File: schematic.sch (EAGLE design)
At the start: 24 parts, among them IC1 ATMEGA168-20P, IC2 7805T, IC3 REG1117

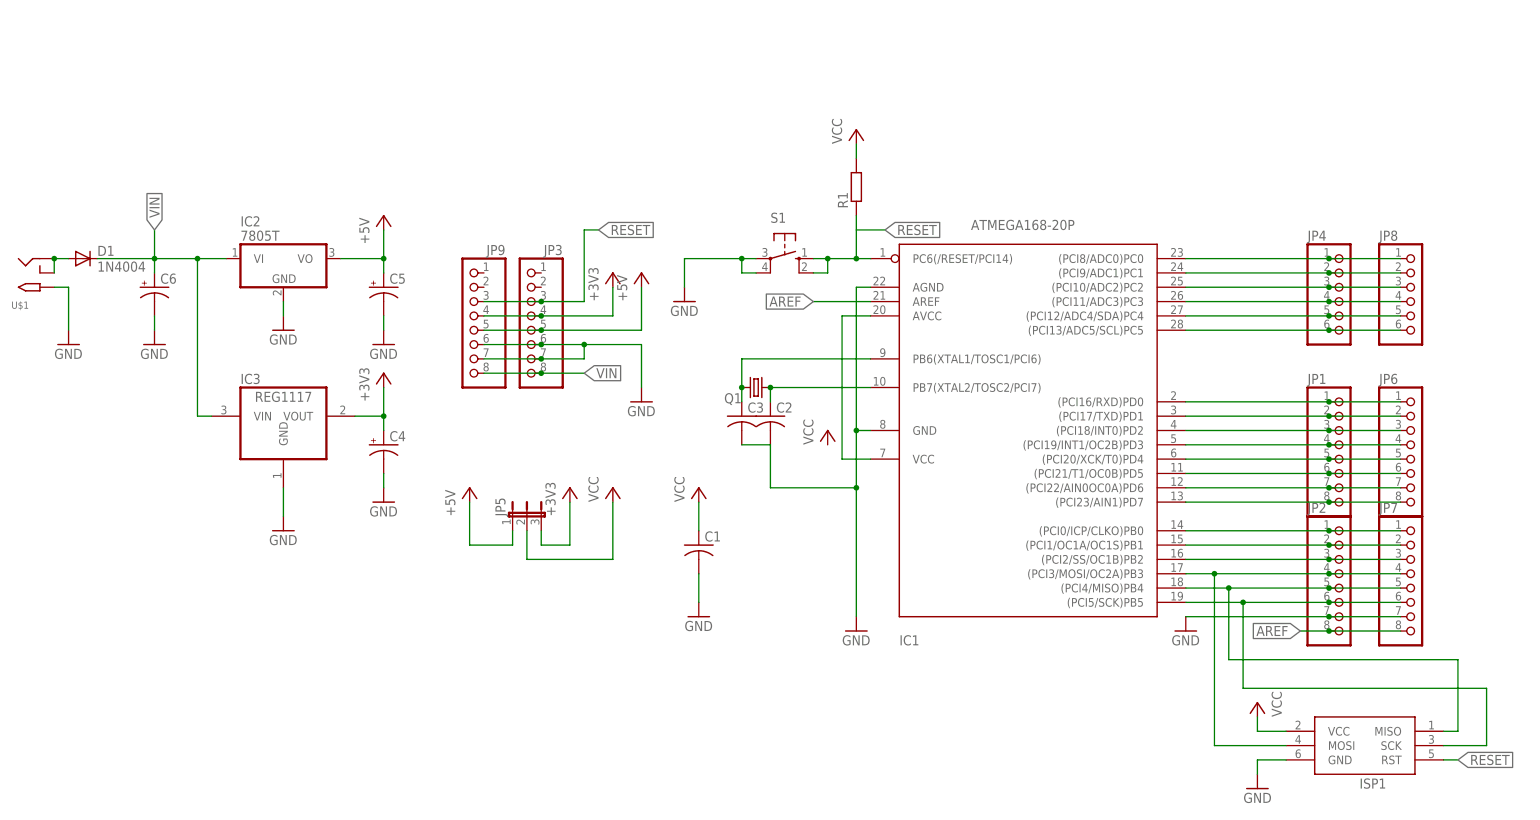
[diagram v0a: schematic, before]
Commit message: Small fixes
Added a serial port header and LEDs for on and pin 13
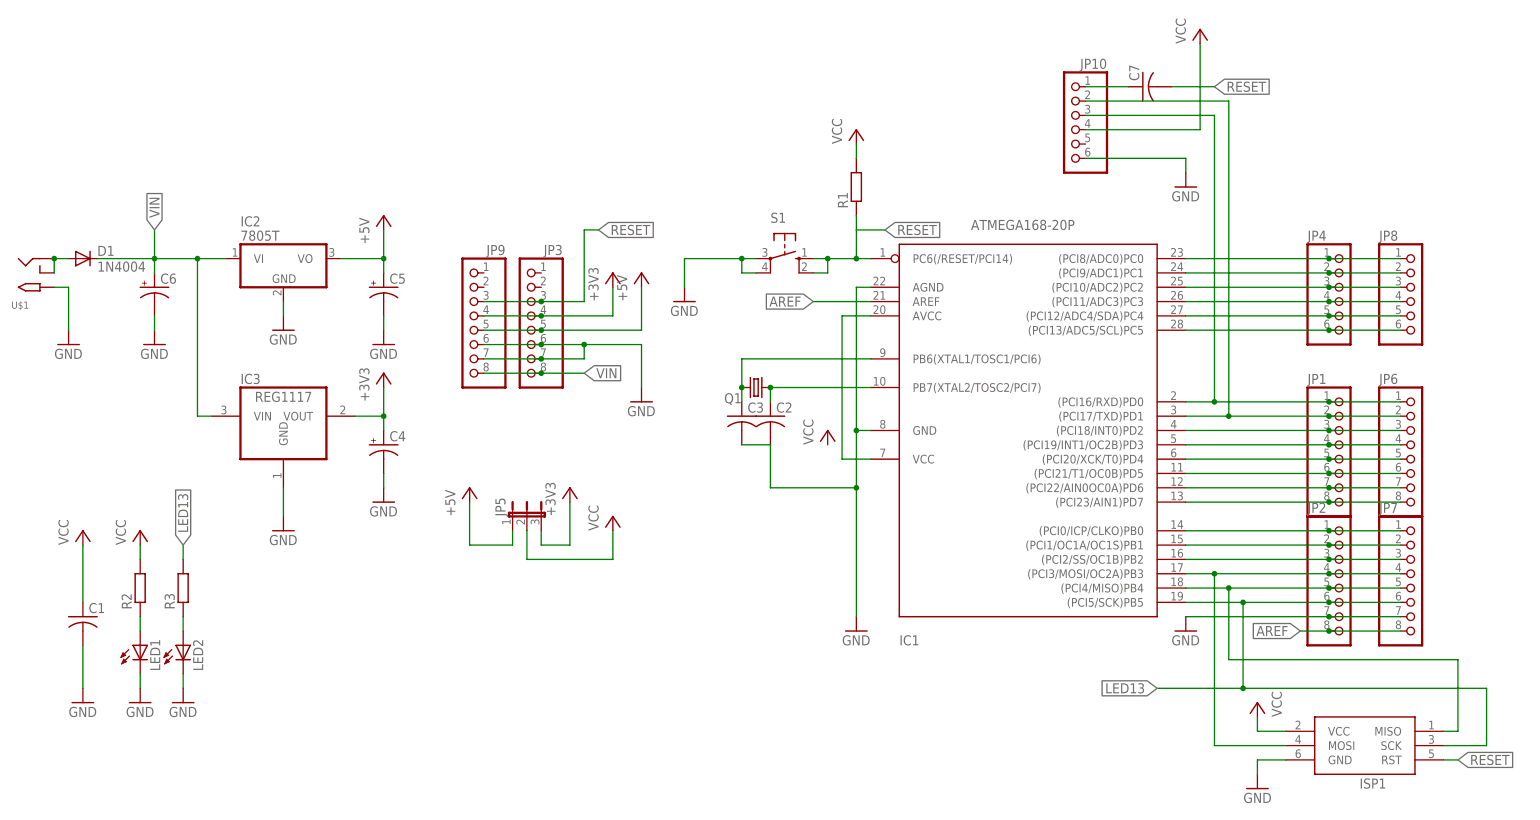
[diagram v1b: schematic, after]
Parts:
- added C7: (no value), adafruit:C-US025-030X050
- added JP10: (no value), adafruit:PINHD-1X6
- added LED1, LED2: (no value), adafruit:LED5MM
- added R2, R3: (no value), rcl:R-EU_0207/7
- JP1, JP3, JP6, JP7, JP9: device adafruit:PINHD-1X8-3.5MM -> adafruit:PINHD-1X8BIG
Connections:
- removed net N$26: IC1.(PCI5/SCK)PB5, ISP1.SCK, JP2.6, JP7.6
- new net LED13: IC1.(PCI5/SCK)PB5, ISP1.SCK, JP2.6, JP7.6, R3.2
- new net N$1: C7.1, JP10.1
- new net N$5: LED1.A, R2.1
- new net N$6: LED2.A, R3.1
- net GND: now also JP10.6, LED1.C, LED2.C
- net N$13: now also JP10.3
- net N$14: now also JP10.2
- net RESET: now also C7.2
- net VCC: now also JP10.4, R2.2
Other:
- moved on the sheet: C1
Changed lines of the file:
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@@
 <part name="IC1" library="adafruit" deviceset="ATMEGA168*P" device="" technology="-20"/>
 <part name="ISP1" library="adafruit" deviceset="AVRISP" device="-6"/>
-<part name="JP1" library="adafruit" deviceset="PINHD-1X8" device="-3.5MM"/>
+<part name="JP1" library="adafruit" deviceset="PINHD-1X8" device="BIG"/>
 <part name="JP2" library="adafruit" deviceset="PINHD-1X8" device="-3.5MM"/>
-<part name="JP3" library="adafruit" deviceset="PINHD-1X8" device="-3.5MM"/>
+<part name="JP3" library="adafruit" deviceset="PINHD-1X8" device="BIG"/>
 <part name="JP4" library="adafruit" deviceset="PINHD-1X6" device=""/>
 <part name="IC2" library="adafruit" deviceset="78*" device="T" technology="05"/>
@@
 <part name="GND10" library="supply1" deviceset="GND" device=""/>
 <part name="GND11" library="supply1" deviceset="GND" device=""/>
-<part name="JP6" library="adafruit" deviceset="PINHD-1X8" device="-3.5MM"/>
-<part name="JP7" library="adafruit" deviceset="PINHD-1X8" device="-3.5MM"/>
+<part name="JP6" library="adafruit" deviceset="PINHD-1X8" device="BIG"/>
+<part name="JP7" library="adafruit" deviceset="PINHD-1X8" device="BIG"/>
 <part name="JP8" library="adafruit" deviceset="PINHD-1X6" device=""/>
-<part name="JP9" library="adafruit" deviceset="PINHD-1X8" device="-3.5MM"/>
+<part name="JP9" library="adafruit" deviceset="PINHD-1X8" device="BIG"/>
 <part name="P+8" library="supply1" deviceset="VCC" device=""/>
 <part name="GND12" library="supply1" deviceset="GND" device=""/>
+<part name="P+9" library="supply1" deviceset="VCC" device=""/>
+<part name="GND13" library="supply1" deviceset="GND" device=""/>
+<part name="JP10" library="adafruit" deviceset="PINHD-1X6" device=""/>
+<part name="C7" library="adafruit" deviceset="C-US" device="025-030X050"/>
+<part name="R2" library="rcl" deviceset="R-EU_" device="0207/7"/>
+<part name="P+10" library="supply1" deviceset="VCC" device=""/>
+<part name="LED1" library="adafruit" deviceset="LED" device="5MM"/>
+<part name="GND14" library="supply1" deviceset="GND" device=""/>
+<part name="R3" library="rcl" deviceset="R-EU_" device="0207/7"/>
+<part name="LED2" library="adafruit" deviceset="LED" device="5MM"/>
+<part name="GND15" library="supply1" deviceset="GND" device=""/>
 </parts>
 <sheets>
@@
 <instance part="Q1" gate="G$1" x="7.62" y="60.96" rot="R180"/>
 <instance part="U$1" gate="G$1" x="-121.92" y="81.28" rot="MR180"/>
-<instance part="C1" gate="G$1" x="-2.54" y="33.02"/>
+<instance part="C1" gate="G$1" x="-111.76" y="20.32"/>
 <instance part="C2" gate="G$1" x="10.16" y="55.88"/>
 <instance part="GND1" gate="1" x="-114.3" y="68.58"/>
@@
 <instance part="P+2" gate="1" x="-43.18" y="43.18"/>
 <instance part="+3V2" gate="G$1" x="-25.4" y="43.18"/>
-<instance part="P+3" gate="VCC" x="-17.78" y="43.18"/>
+<instance part="P+3" gate="VCC" x="-17.78" y="38.1"/>
 <instance part="P+4" gate="VCC" x="20.32" y="53.34"/>
 <instance part="GND4" gate="1" x="25.4" y="17.78"/>
@@
 <instance part="+3V3" gate="G$1" x="-17.78" y="81.28"/>
 <instance part="P+6" gate="1" x="-12.7" y="81.28"/>
-<instance part="P+7" gate="VCC" x="-2.54" y="43.18"/>
-<instance part="GND8" gate="1" x="-2.54" y="20.32"/>
+<instance part="P+7" gate="VCC" x="-111.76" y="35.56"/>
+<instance part="GND8" gate="1" x="-111.76" y="5.08"/>
 <instance part="C4" gate="G$1" x="-58.42" y="50.8"/>
 <instance part="C5" gate="G$1" x="-58.42" y="78.74"/>
@@
 <instance part="P+8" gate="VCC" x="96.52" y="5.08" rot="MR0"/>
 <instance part="GND12" gate="1" x="96.52" y="-10.16" rot="MR0"/>
+<instance part="P+9" gate="VCC" x="86.36" y="124.46"/>
+<instance part="GND13" gate="1" x="83.82" y="96.52"/>
+<instance part="JP10" gate="A" x="63.5" y="106.68" rot="MR0"/>
+<instance part="C7" gate="G$1" x="76.2" y="114.3" rot="R90"/>
+<instance part="R2" gate="G$1" x="-101.6" y="25.4" rot="R90"/>
+<instance part="P+10" gate="VCC" x="-101.6" y="35.56"/>
+<instance part="LED1" gate="G$1" x="-101.6" y="15.24"/>
+<instance part="GND14" gate="1" x="-101.6" y="5.08"/>
+<instance part="R3" gate="G$1" x="-93.98" y="25.4" rot="R90"/>
+<instance part="LED2" gate="G$1" x="-93.98" y="15.24"/>
+<instance part="GND15" gate="1" x="-93.98" y="5.08"/>
 </instances>
 <busses>
@@
 <pinref part="GND8" gate="1" pin="GND"/>
 <pinref part="C1" gate="G$1" pin="2"/>
-<wire x1="-2.54" y1="22.86" x2="-2.54" y2="27.94" width="0.1524" layer="91"/>
+<wire x1="-111.76" y1="7.62" x2="-111.76" y2="15.24" width="0.1524" layer="91"/>
 </segment>
 <segment>
@@
 <wire x1="101.6" y1="-5.08" x2="96.52" y2="-5.08" width="0.1524" layer="91"/>
 <wire x1="96.52" y1="-5.08" x2="96.52" y2="-7.62" width="0.1524" layer="91"/>
+</segment>
+<segment>
+<pinref part="GND13" gate="1" pin="GND"/>
+<wire x1="83.82" y1="101.6" x2="83.82" y2="99.06" width="0.1524" layer="91"/>
+<pinref part="JP10" gate="A" pin="6"/>
+<wire x1="66.04" y1="101.6" x2="83.82" y2="101.6" width="0.1524" layer="91"/>
+</segment>
+<segment>
+<pinref part="GND14" gate="1" pin="GND"/>
+<pinref part="LED1" gate="G$1" pin="C"/>
+<wire x1="-101.6" y1="7.62" x2="-101.6" y2="10.16" width="0.1524" layer="91"/>
+</segment>
+<segment>
+<pinref part="GND15" gate="1" pin="GND"/>
+<pinref part="LED2" gate="G$1" pin="C"/>
+<wire x1="-93.98" y1="7.62" x2="-93.98" y2="10.16" width="0.1524" layer="91"/>
 </segment>
 </net>
@@
 <wire x1="-33.02" y1="35.56" x2="-33.02" y2="30.48" width="0.1524" layer="91"/>
 <wire x1="-33.02" y1="30.48" x2="-17.78" y2="30.48" width="0.1524" layer="91"/>
-<wire x1="-17.78" y1="30.48" x2="-17.78" y2="40.64" width="0.1524" layer="91"/>
+<wire x1="-17.78" y1="30.48" x2="-17.78" y2="35.56" width="0.1524" layer="91"/>
 <pinref part="P+3" gate="VCC" pin="VCC"/>
 </segment>
@@
 <pinref part="C1" gate="G$1" pin="1"/>
 <pinref part="P+7" gate="VCC" pin="VCC"/>
-<wire x1="-2.54" y1="35.56" x2="-2.54" y2="40.64" width="0.1524" layer="91"/>
+<wire x1="-111.76" y1="22.86" x2="-111.76" y2="33.02" width="0.1524" layer="91"/>
 </segment>
 <segment>
@@
 <wire x1="101.6" y1="0" x2="96.52" y2="0" width="0.1524" layer="91"/>
 <wire x1="96.52" y1="0" x2="96.52" y2="2.54" width="0.1524" layer="91"/>
+</segment>
+<segment>
+<pinref part="P+9" gate="VCC" pin="VCC"/>
+<pinref part="JP10" gate="A" pin="4"/>
+<wire x1="86.36" y1="106.68" x2="86.36" y2="121.92" width="0.1524" layer="91"/>
+<wire x1="66.04" y1="106.68" x2="86.36" y2="106.68" width="0.1524" layer="91"/>
+</segment>
+<segment>
+<pinref part="R2" gate="G$1" pin="2"/>
+<pinref part="P+10" gate="VCC" pin="VCC"/>
+<wire x1="-101.6" y1="30.48" x2="-101.6" y2="33.02" width="0.1524" layer="91"/>
 </segment>
 </net>
@@
 <label x="132.08" y="-5.08" size="1.778" layer="95" xref="yes"/>
 </segment>
+<segment>
+<pinref part="C7" gate="G$1" pin="2"/>
+<wire x1="81.28" y1="114.3" x2="88.9" y2="114.3" width="0.1524" layer="91"/>
+<label x="88.9" y="114.3" size="1.778" layer="95" rot="MR180" xref="yes"/>
+</segment>
 </net>
 <net name="N$7" class="0">
@@
 <pinref part="IC1" gate="G$1" pin="(PCI16/RXD)PD0"/>
 <pinref part="JP1" gate="G$1" pin="1"/>
-<wire x1="83.82" y1="58.42" x2="109.22" y2="58.42" width="0.1524" layer="91"/>
+<wire x1="83.82" y1="58.42" x2="88.9" y2="58.42" width="0.1524" layer="91"/>
 <pinref part="JP6" gate="G$1" pin="1"/>
+<wire x1="88.9" y1="58.42" x2="109.22" y2="58.42" width="0.1524" layer="91"/>
 <wire x1="121.92" y1="58.42" x2="109.22" y2="58.42" width="0.1524" layer="91"/>
 <junction x="109.22" y="58.42"/>
+<wire x1="88.9" y1="109.22" x2="88.9" y2="58.42" width="0.1524" layer="91"/>
+<junction x="88.9" y="58.42"/>
+<pinref part="JP10" gate="A" pin="3"/>
+<wire x1="66.04" y1="109.22" x2="88.9" y2="109.22" width="0.1524" layer="91"/>
 </segment>
 </net>
@@
 <pinref part="IC1" gate="G$1" pin="(PCI17/TXD)PD1"/>
 <pinref part="JP1" gate="G$1" pin="2"/>
-<wire x1="83.82" y1="55.88" x2="109.22" y2="55.88" width="0.1524" layer="91"/>
+<wire x1="83.82" y1="55.88" x2="91.44" y2="55.88" width="0.1524" layer="91"/>
 <pinref part="JP6" gate="G$1" pin="2"/>
+<wire x1="91.44" y1="55.88" x2="109.22" y2="55.88" width="0.1524" layer="91"/>
 <wire x1="109.22" y1="55.88" x2="121.92" y2="55.88" width="0.1524" layer="91"/>
 <junction x="109.22" y="55.88"/>
+<wire x1="91.44" y1="55.88" x2="91.44" y2="111.76" width="0.1524" layer="91"/>
+<junction x="91.44" y="55.88"/>
+<pinref part="JP10" gate="A" pin="2"/>
+<wire x1="66.04" y1="111.76" x2="91.44" y2="111.76" width="0.1524" layer="91"/>
 </segment>
 </net>
@@
 </segment>
 </net>
-<net name="N$26" class="0">
+<net name="LED13" class="0">
 <segment>
 <pinref part="JP2" gate="G$1" pin="6"/>
@@
 <wire x1="93.98" y1="7.62" x2="93.98" y2="22.86" width="0.1524" layer="91"/>
 <junction x="93.98" y="22.86"/>
+<wire x1="93.98" y1="7.62" x2="78.74" y2="7.62" width="0.1524" layer="91"/>
+<junction x="93.98" y="7.62"/>
+<label x="78.74" y="7.62" size="1.778" layer="95" rot="MR0" xref="yes"/>
+</segment>
+<segment>
+<pinref part="R3" gate="G$1" pin="2"/>
+<wire x1="-93.98" y1="30.48" x2="-93.98" y2="33.02" width="0.1524" layer="91"/>
+<label x="-93.98" y="33.02" size="1.778" layer="95" rot="R90" xref="yes"/>
 </segment>
 </net>
@@
 </segment>
 </net>
+<net name="N$1" class="0">
+<segment>
+<pinref part="C7" gate="G$1" pin="1"/>
+<pinref part="JP10" gate="A" pin="1"/>
+<wire x1="73.66" y1="114.3" x2="66.04" y2="114.3" width="0.1524" layer="91"/>
+</segment>
+</net>
+<net name="N$5" class="0">
+<segment>
+<pinref part="LED1" gate="G$1" pin="A"/>
+<pinref part="R2" gate="G$1" pin="1"/>
+<wire x1="-101.6" y1="17.78" x2="-101.6" y2="20.32" width="0.1524" layer="91"/>
+</segment>
+</net>
+<net name="N$6" class="0">
+<segment>
+<pinref part="LED2" gate="G$1" pin="A"/>
+<pinref part="R3" gate="G$1" pin="1"/>
+<wire x1="-93.98" y1="17.78" x2="-93.98" y2="20.32" width="0.1524" layer="91"/>
+</segment>
+</net>

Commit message: Fixes in net names and the voltage input jack
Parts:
- C1, C7: device adafruit:C-US025-030X050 -> resistor:C-EU050-025X075
- JP2: device adafruit:PINHD-1X8-3.5MM -> adafruit:PINHD-1X8BIG
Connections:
- removed net N$4: IC1.AVCC, IC1.VCC
- new net VD: C6.+, D1.C, IC2.VI, IC3.VIN
- net GND: now also U$1.RING, U$1.RING_SW; no longer U$1.TIP
- net VCC: now also IC1.AVCC, IC1.VCC
- net VIN: now also U$1.TIP; no longer C6.+, D1.C, IC2.VI, IC3.VIN, U$1.RING, U$1.RING_SW
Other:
- moved on the sheet: U$1
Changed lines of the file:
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@@
 <part name="ISP1" library="adafruit" deviceset="AVRISP" device="-6"/>
 <part name="JP1" library="adafruit" deviceset="PINHD-1X8" device="BIG"/>
-<part name="JP2" library="adafruit" deviceset="PINHD-1X8" device="-3.5MM"/>
+<part name="JP2" library="adafruit" deviceset="PINHD-1X8" device="BIG"/>
 <part name="JP3" library="adafruit" deviceset="PINHD-1X8" device="BIG"/>
 <part name="JP4" library="adafruit" deviceset="PINHD-1X6" device=""/>
@@
 <part name="Q1" library="adafruit" deviceset="CRYSTAL" device="HC49S"/>
 <part name="U$1" library="adafruit" deviceset="2.1MMJACK" device="THM"/>
-<part name="C1" library="adafruit" deviceset="C-US" device="025-030X050"/>
+<part name="C1" library="resistor" deviceset="C-EU" device="050-025X075"/>
 <part name="C2" library="adafruit" deviceset="C-US" device="025-030X050"/>
 <part name="GND1" library="supply1" deviceset="GND" device=""/>
@@
 <part name="GND13" library="supply1" deviceset="GND" device=""/>
 <part name="JP10" library="adafruit" deviceset="PINHD-1X6" device=""/>
-<part name="C7" library="adafruit" deviceset="C-US" device="025-030X050"/>
+<part name="C7" library="resistor" deviceset="C-EU" device="050-025X075"/>
 <part name="R2" library="rcl" deviceset="R-EU_" device="0207/7"/>
 <part name="P+10" library="supply1" deviceset="VCC" device=""/>
@@
 <instance part="IC3" gate="G$1" x="-76.2" y="55.88"/>
 <instance part="Q1" gate="G$1" x="7.62" y="60.96" rot="R180"/>
-<instance part="U$1" gate="G$1" x="-121.92" y="81.28" rot="MR180"/>
+<instance part="U$1" gate="G$1" x="-121.92" y="81.28"/>
 <instance part="C1" gate="G$1" x="-111.76" y="20.32"/>
 <instance part="C2" gate="G$1" x="10.16" y="55.88"/>
@@
 </segment>
 <segment>
-<pinref part="U$1" gate="G$1" pin="TIP"/>
 <pinref part="GND1" gate="1" pin="GND"/>
+<wire x1="-114.3" y1="78.74" x2="-114.3" y2="71.12" width="0.1524" layer="91"/>
+<pinref part="U$1" gate="G$1" pin="RING"/>
+<pinref part="U$1" gate="G$1" pin="RING_SW"/>
+<wire x1="-116.84" y1="81.28" x2="-116.84" y2="78.74" width="0.1524" layer="91"/>
 <wire x1="-116.84" y1="78.74" x2="-114.3" y2="78.74" width="0.1524" layer="91"/>
-<wire x1="-114.3" y1="78.74" x2="-114.3" y2="71.12" width="0.1524" layer="91"/>
+<junction x="-116.84" y="78.74"/>
 </segment>
 <segment>
@@
 <wire x1="-101.6" y1="30.48" x2="-101.6" y2="33.02" width="0.1524" layer="91"/>
 </segment>
+<segment>
+<pinref part="P+4" gate="VCC" pin="VCC"/>
+<wire x1="20.32" y1="50.8" x2="20.32" y2="48.26" width="0.1524" layer="91"/>
+<pinref part="IC1" gate="G$1" pin="VCC"/>
+<wire x1="27.94" y1="48.26" x2="22.86" y2="48.26" width="0.1524" layer="91"/>
+<wire x1="22.86" y1="48.26" x2="22.86" y2="73.66" width="0.1524" layer="91"/>
+<pinref part="IC1" gate="G$1" pin="AVCC"/>
+<wire x1="22.86" y1="73.66" x2="27.94" y2="73.66" width="0.1524" layer="91"/>
+<wire x1="20.32" y1="48.26" x2="22.86" y2="48.26" width="0.1524" layer="91"/>
+<junction x="22.86" y="48.26"/>
+</segment>
 </net>
 <net name="N$2" class="0">
@@
 <wire x1="10.16" y1="58.42" x2="10.16" y2="60.96" width="0.1524" layer="91"/>
 <junction x="10.16" y="60.96"/>
-</segment>
-</net>
-<net name="N$4" class="0">
-<segment>
-<pinref part="IC1" gate="G$1" pin="VCC"/>
-<wire x1="27.94" y1="48.26" x2="22.86" y2="48.26" width="0.1524" layer="91"/>
-<wire x1="22.86" y1="48.26" x2="22.86" y2="73.66" width="0.1524" layer="91"/>
-<pinref part="IC1" gate="G$1" pin="AVCC"/>
-<wire x1="22.86" y1="73.66" x2="27.94" y2="73.66" width="0.1524" layer="91"/>
 </segment>
 </net>
@@
 </segment>
 </net>
-<net name="VIN" class="0">
-<segment>
-<pinref part="U$1" gate="G$1" pin="RING"/>
-<pinref part="U$1" gate="G$1" pin="RING_SW"/>
-<wire x1="-116.84" y1="81.28" x2="-116.84" y2="83.82" width="0.1524" layer="91"/>
-<pinref part="D1" gate="1" pin="A"/>
-<wire x1="-114.3" y1="83.82" x2="-116.84" y2="83.82" width="0.1524" layer="91"/>
-<junction x="-116.84" y="83.82"/>
-</segment>
-<segment>
-<pinref part="JP3" gate="G$1" pin="8"/>
-<wire x1="-30.48" y1="63.5" x2="-22.86" y2="63.5" width="0.1524" layer="91"/>
-<label x="-22.86" y="63.5" size="1.778" layer="95" xref="yes"/>
-<pinref part="JP9" gate="G$1" pin="8"/>
-<wire x1="-30.48" y1="63.5" x2="-40.64" y2="63.5" width="0.1524" layer="91"/>
-<junction x="-30.48" y="63.5"/>
-</segment>
+<net name="VD" class="0">
 <segment>
 <pinref part="IC2" gate="A1" pin="VI"/>
@@
 <wire x1="-91.44" y1="55.88" x2="-91.44" y2="83.82" width="0.1524" layer="91"/>
 <junction x="-91.44" y="83.82"/>
-<label x="-99.06" y="88.9" size="1.778" layer="95" rot="R90" xref="yes"/>
-<wire x1="-99.06" y1="83.82" x2="-99.06" y2="88.9" width="0.1524" layer="91"/>
+<label x="-99.06" y="83.82" size="1.778" layer="95" rot="R90" xref="yes"/>
 </segment>
 </net>
@@
 </segment>
 </net>
+<net name="VIN" class="0">
+<segment>
+<pinref part="U$1" gate="G$1" pin="TIP"/>
+<pinref part="D1" gate="1" pin="A"/>
+<wire x1="-116.84" y1="83.82" x2="-114.3" y2="83.82" width="0.1524" layer="91"/>
+<wire x1="-114.3" y1="83.82" x2="-114.3" y2="88.9" width="0.1524" layer="91"/>
+<junction x="-114.3" y="83.82"/>
+<label x="-114.3" y="88.9" size="1.778" layer="95" rot="R90" xref="yes"/>
+</segment>
+<segment>
+<pinref part="JP3" gate="G$1" pin="8"/>
+<wire x1="-30.48" y1="63.5" x2="-22.86" y2="63.5" width="0.1524" layer="91"/>
+<label x="-22.86" y="63.5" size="1.778" layer="95" xref="yes"/>
+<pinref part="JP9" gate="G$1" pin="8"/>
+<wire x1="-30.48" y1="63.5" x2="-40.64" y2="63.5" width="0.1524" layer="91"/>
+<junction x="-30.48" y="63.5"/>
+</segment>
+</net>
